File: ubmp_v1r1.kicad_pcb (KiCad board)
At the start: 2 copper layers, 38.5 x 12 mm, 24 parts, among them J1 USB_A, J2 Conn_02x04_Top_Bottom, U1 STM32F103CBUx, U2 MIC5245-3.3, Y1 PRQC8.00CR1010V00L

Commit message: PCB layout
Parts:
- moved R7 1.00 mm to (105.2, 110.6)
- moved R9 1.00 mm to (105.2, 109.6)
- moved C6 0.40 mm to (102.4, 106.5), turned to 270 degrees
- moved U2 0.20 mm to (99.7, 106.5), turned to 0 degrees
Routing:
- net +5V: track 0.00 -> 42.0 mm
- net +3V3: track 10.8 -> 47.4 mm, vias 0 -> 3
- net GND: track 26.2 -> 42.6 mm, vias 5 -> 15
- net Net-(J2-Pad3): track 0.00 -> 10.9 mm, vias 0 -> 1
- net Net-(J2-Pad2): track 0.00 -> 10.3 mm, vias 0 -> 1
- net Net-(J2-Pad8): track 0.00 -> 9.62 mm
- net Net-(J2-Pad4): track 0.00 -> 9.54 mm, vias 0 -> 1
- net Net-(J2-Pad7): track 0.00 -> 9.40 mm
- net Net-(J2-Pad6): track 0.00 -> 9.07 mm
- net /BMP_RX: track 8.49 -> 14.6 mm, vias 1 -> 3
- net /BMP_TX: track 8.03 -> 11.5 mm, vias 1 -> 3
- net Net-(D1-Pad2): track 0.00 -> 1.35 mm
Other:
- net class Power added: clearance 0.2, trace_width 0.2, via_dia 0.6, via_drill 0.3
- board text added: "GND"

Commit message: PCB layout done
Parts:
- C1, C2, C3, C4, R1, R10, R11, R12, R2, R7, R8, R9, U1, Y1: moved to F.Cu
- J2: moved to B.Cu
- moved R1 10.1 mm to (100.0, 101.1)
- moved R6 10.1 mm to (94.0, 110.7), turned to 0 degrees
- moved R5 10.1 mm to (94.0, 109.7), turned to 0 degrees
- moved C6 9.56 mm to (94.3, 101.5), turned to 0 degrees
- moved Y1 9.53 mm to (103.0, 101.4)
- moved R7 9.34 mm to (107.2, 101.5)
- moved R3 8.85 mm to (96.8, 103.1), turned to 270 degrees
- moved C2 8.52 mm to (107.2, 110.2)
- moved C3 8.21 mm to (97.0, 109.0), turned to 90 degrees
- moved C1 8.17 mm to (100.0, 102.1)
- moved R4 7.92 mm to (94.0, 108.7), turned to 0 degrees
- moved R9 7.40 mm to (107.2, 102.5)
- moved R11 6.59 mm to (107.2, 109.2)
- moved U2 5.91 mm to (94.3, 104.2), turned to 90 degrees
- moved D1 5.51 mm to (96.8, 105.5), turned to 90 degrees
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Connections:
- net Net-(R3-Pad1) renamed /LED
- net Net-(R4-Pad2) renamed /DPU
- net Net-(R5-Pad2) renamed /DM_P
- net Net-(R6-Pad2) renamed /DP_P
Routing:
- net /BMP_RX: track 14.6 -> 30.0 mm
- net +5V: track 42.0 -> 51.6 mm, vias 0 -> 5
- net /DM: track 19.0 -> 10.3 mm
- net /BMP_TX: track 11.5 -> 19.1 mm
- net /LED: track 3.87 -> 11.3 mm, vias 1 -> 2
- net /DP_P: track 2.48 -> 9.93 mm, vias 1 -> 0
- net /DPU: track 2.79 -> 9.01 mm, vias 1 -> 0
- net /DM_P: track 5.19 -> 9.48 mm, vias 1 -> 0
- net /DP: track 17.1 -> 13.4 mm, vias 0 -> 2
- net +3V3: track 47.4 -> 46.1 mm, vias 3 -> 4
- net GND: track 42.6 -> 43.9 mm, vias 15 -> 23
- net Net-(J2-Pad4): track 9.54 -> 10.4 mm
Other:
- board size 38.5 x 12 mm -> 40.5 x 12 mm
- net class Power removed

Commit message: Added text to PCB
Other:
- board text added: "Emil Fresk"
- board text added: "USB"
- board text added: "µBMP v1.0"
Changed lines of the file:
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@@
   (general
     (thickness 1.6)
-    (drawings 18)
+    (drawings 21)
     (tracks 325)
     (zones 0)
@@
     (46 B.CrtYd user)
     (47 F.CrtYd user)
-    (48 B.Fab user hide)
+    (48 B.Fab user)
     (49 F.Fab user)
   )
@@
     (pad_to_mask_clearance 0.08)
     (aux_axis_origin 0 0)
-    (visible_elements FFFFFF3F)
+    (visible_elements FFF9FF9F)
     (pcbplotparams
       (layerselection 0x010fc_ffffffff)
@@
   (module usbpcb:USBPCB (layer F.Cu)
     (at 84.5 106 90)
-    (fp_text reference J1 (at 0 -8.89 90) (layer F.SilkS)
+    (fp_text reference J1 (at 0 -8.89 90) (layer F.SilkS) hide
       (effects (font (size 0.7 0.7) (thickness 0.15)))
     )
@@
   (module ubmp:2x5_2.54mm_side (layer B.Cu)
     (at 116.2 105.995364 270)
-    (fp_text reference J2 (at 0 -2.54 270) (layer B.SilkS)
+    (fp_text reference J2 (at 0 -2.54 270) (layer B.SilkS) hide
       (effects (font (size 0.7 0.7) (thickness 0.15)) (justify mirror))
     )
@@
     )
   )
+  (gr_text USB (at 90.125 106.1 90) (layer F.SilkS)
+    (effects (font (size 1.5 1.5) (thickness 0.3)))
+  )
+  (gr_text "Emil Fresk" (at 100.9 109.2) (layer B.SilkS)
+    (effects (font (size 1.2 1.2) (thickness 0.25)) (justify mirror))
+  )
+  (gr_text "µBMP v1.0" (at 99.625 106.9) (layer B.SilkS)
+    (effects (font (size 1.5 1.5) (thickness 0.3)) (justify mirror))
+  )
   (gr_text GND (at 112.3 102.095364) (layer F.SilkS)

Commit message: Added text to PCB
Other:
- board text added: "µBMP"
- board text removed: "USB"
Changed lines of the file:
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@@
     )
   )
-  (gr_text USB (at 90.125 106.1 90) (layer F.SilkS)
+  (gr_text µBMP (at 89.95 106.1 90) (layer F.SilkS)
     (effects (font (size 1.5 1.5) (thickness 0.3)))
   )

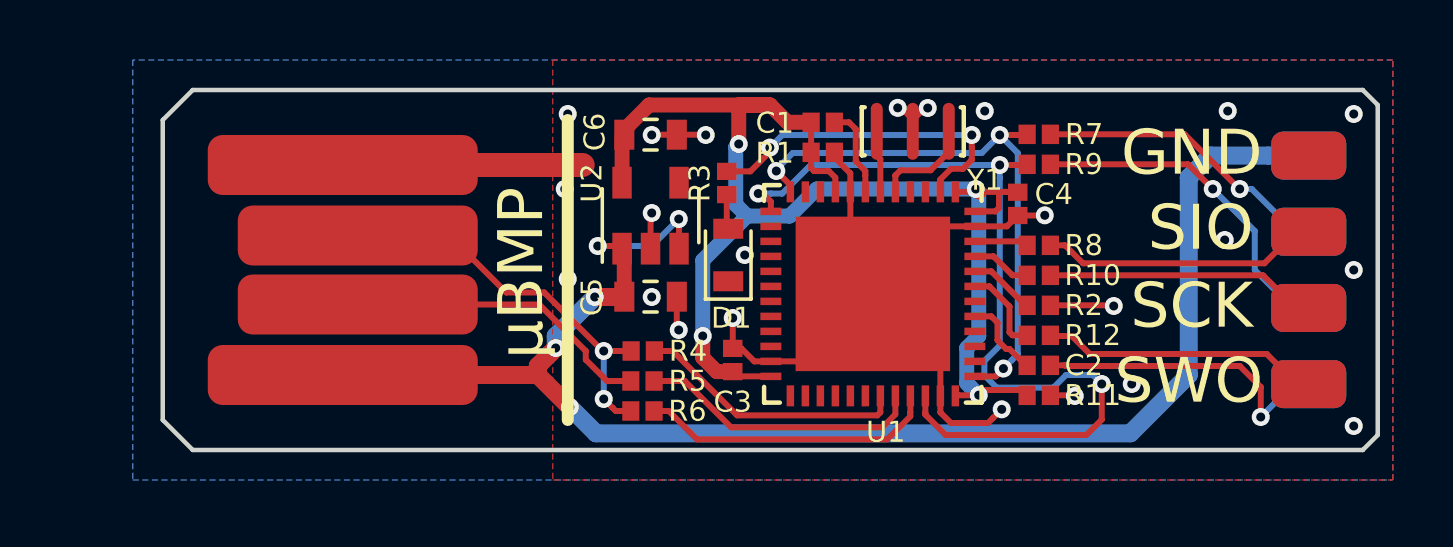
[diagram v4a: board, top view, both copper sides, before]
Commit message: More GND
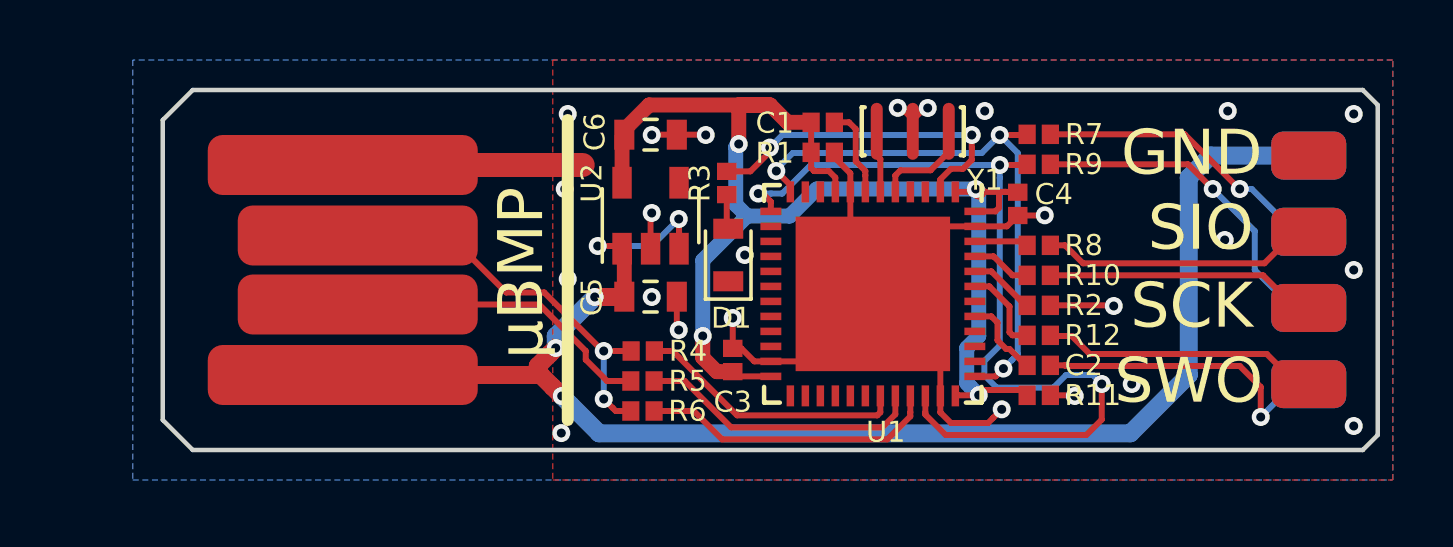
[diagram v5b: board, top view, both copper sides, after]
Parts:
- added REF**: OSHW-Symbol_8.9x8mm_SilkScreen, Symbol:OSHW-Symbol_8.9x8mm_SilkScreen, B.Cu at (85.0, 106.0)
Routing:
- net GND: vias 23 -> 24
